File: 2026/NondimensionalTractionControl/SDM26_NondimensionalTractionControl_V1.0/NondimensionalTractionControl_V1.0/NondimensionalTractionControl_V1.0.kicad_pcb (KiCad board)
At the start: 4 copper layers, 50 x 50 mm, 52 parts, among them IC1 STM32H743VIT6, IC2 74LVC1G17SE-7, IC3 TLP175A_TPL,E, IC4 SN65HVD230QDR, IC5 TPS259250DRCR, IC6 MIC37100-3.3WS, IC7 TPS2116DRLR, J1 104031-0811, J2 Conn_ARM_SWD_TagConnect_TC203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, J3 105017-0001, J4 SM04B-ULHK-1TA1-ETB_HF_, J5 SM04B-ULHK-1TA1-ETB_HF_, J6 SM04B-ULHK-1TA1-ETB_HF_, U1 USBLC6-2SC6, Y1 ABM3B-8.000MHZ-10-1-U-T

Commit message: NDTC PCB mostly done
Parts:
- added R12: 10k, Resistor_SMD:R_0603_1608Metric, F.Cu at (158.6, 137.3)
- J3: value 105017-0001 -> USB_B_Micro
- moved R4 81.6 mm to (103.9, 116.3), turned to 180 degrees
- moved J6 66.8 mm to (165.6, 144.2), turned to -90 degrees
- moved C15 65.5 mm to (132.4, 149.0), turned to 180 degrees
- moved C16 61.3 mm to (135.8, 149.0), turned to 180 degrees
- moved C19 57.8 mm to (132.3, 123.3)
- moved R1 57.8 mm to (132.3, 128.3)
- moved C8 55.5 mm to (144.2, 147.5)
- moved C9 54.7 mm to (144.2, 149.0)
- moved R3 54.1 mm to (146.5, 148.2), turned to 90 degrees
- moved R11 53.9 mm to (103.9, 120.2), turned to 180 degrees
- moved R5 50.7 mm to (148.9, 131.0), turned to 180 degrees
- moved R2 43.8 mm to (157.7, 142.0)
- moved R8 43.2 mm to (151.9, 140.6)
- moved C4 43.1 mm to (138.2, 133.0), turned to -90 degrees
- moved C20 41.7 mm to (153.4, 134.2), turned to 180 degrees
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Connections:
- IC1 pad 1: WheelSpeed_2 -> WheelSpeed_3
- IC1 pad 2: WheelSpeed_3 -> WheelSpeed_4
- IC1 pad 3: WheelSpeed_4 -> unconnected-(IC1-PE4-Pad3)
- IC1 pad 51: Net-(IC1-PB12) -> /FDCAN2_RX
- IC1 pad 52: unconnected-(IC1-PB13-Pad52) -> /FDCAN2_TX
- IC1 pad 53: unconnected-(IC1-PB14-Pad53) -> /CAN_TERM
- IC1 pad 54: unconnected-(IC1-PB15-Pad54) -> /USER_LED
- IC1 pad 95: /FDCAN1_RX -> unconnected-(IC1-PB8-Pad95)
- IC1 pad 96: /FDCAN1_TX -> unconnected-(IC1-PB9-Pad96)
- IC1 pad 97: /CAN_TERM -> WheelSpeed_1
- IC1 pad 98: WheelSpeed_1 -> WheelSpeed_2
- IC4 pad 1: /FDCAN1_RX -> /FDCAN2_RX
- IC4 pad 4: /FDCAN1_TX -> /FDCAN2_TX
- IC7 pad 4: GND -> Net-(IC7-PR1)
- J6 pad 1: VCC -> GND
- J6 pad 2: /CAN_HI -> /CAN_LOW
- J6 pad 3: /CAN_LOW -> /CAN_HI
- J6 pad 4: GND -> VCC
- R4 pad 1: Net-(IC1-PB12) -> /USER_LED
- R7 pad 2: GND -> Net-(IC7-PR1)
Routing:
- net GND: track 37.8 -> 100.4 mm, vias 45 -> 73
- net VBUS: track 0.00 -> 37.8 mm, vias 0 -> 3
- net /CAN_HI: track 0.00 -> 16.9 mm
- net /CAN_LOW: track 0.00 -> 16.9 mm
- net +3.3V: track 22.3 -> 37.4 mm, vias 5 -> 11
- net /CAN_TERM: track 0.00 -> 14.3 mm
- net /USB_OTG_DP: track 0.00 -> 13.4 mm
- net /USB_OTG_DM: track 0.00 -> 13.0 mm
- net VCC: track 0.00 -> 12.8 mm
- net Net-(R6-Pad2): track 0.00 -> 12.8 mm
- net Net-(R5-Pad1): track 0.00 -> 12.6 mm
- net +5V: track 0.00 -> 8.76 mm
- net /FDCAN2_RX: track 0.00 -> 8.34 mm
- net Net-(IC4-Rs): track 0.00 -> 6.58 mm
- net Net-(IC7-ST): track 0.00 -> 6.41 mm, vias 0 -> 2
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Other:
- board size 50 x 50 mm -> 70 x 35 mm

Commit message: Computer Sync
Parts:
- added LED3: 150060RS75000, SDM_MiscFootprint:LEDC1608X80N, F.Cu at (155.2, 116.6)
- added R13: 150, Resistor_SMD:R_0603_1608Metric, F.Cu at (155.9, 119.1)
- moved J2 30.5 mm to (175.8, 123.3)
- moved C19 19.0 mm to (148.9, 132.5)
- moved FL1 13.6 mm to (155.8, 123.4), turned to -90 degrees
- moved TP1 7.25 mm to (138.3, 117.1)
- moved R1 3.77 mm to (128.6, 128.9), turned to -90 degrees
- moved R5 1.50 mm to (148.9, 129.5)
- moved R6 1.50 mm to (148.9, 131.0)
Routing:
- net /SDMMC1_CD: track 0.00 -> 37.0 mm
- net /SDMMC1_CMD: track 0.00 -> 28.0 mm
- net /SDMMC1_CK: track 0.00 -> 26.3 mm
- net /SDMMC1_D0: track 0.00 -> 25.6 mm, vias 0 -> 2
- net /SDMMC1_D1: track 0.00 -> 24.9 mm, vias 0 -> 2
- net Net-(FL1-DAT2_EX): track 0.00 -> 13.7 mm
- net Net-(FL1-DAT3_EX): track 0.00 -> 13.4 mm
- net Net-(FL1-DAT1_EX): track 0.00 -> 13.3 mm
- net Net-(FL1-CMD_EX): track 0.00 -> 13.1 mm
- net Net-(FL1-DAT0_EX): track 0.00 -> 13.1 mm
- net Net-(FL1-CLK_EX): track 0.00 -> 12.4 mm
- net +3.3V: track 37.4 -> 43.0 mm, vias 11 -> 14
- net GND: track 100.4 -> 104.9 mm, vias 73 -> 78
- net Net-(IC1-BOOT0): track 2.52 -> 5.03 mm
- net Net-(IC7-ST): track 6.41 -> 8.51 mm
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
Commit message: NTC First Rev Complete
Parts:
- added C21: 100nF, Capacitor_SMD:C_0603_1608Metric, F.Cu at (128.6, 125.9)
- added R14: 10k, Resistor_SMD:R_0603_1608Metric, F.Cu at (139.3, 140.8)
- moved LED2 50.4 mm to (151.7, 116.6), turned to 0 degrees
- moved R11 48.7 mm to (152.6, 119.0), turned to 90 degrees
- moved J2 44.6 mm to (131.4, 126.3), turned to -90 degrees
- moved TP1 17.8 mm to (153.3, 126.6)
- moved C12 0.50 mm to (163.1, 136.6)
- moved IC4 0.10 mm to (144.2, 144.0)
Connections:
- IC1 pad 54: /USER_LED -> unconnected-(IC1-PB15-Pad54)
- IC1 pad 92: unconnected-(IC1-PB6-Pad92) -> /USER_LED
- IC4 pad 1: /FDCAN2_RX -> /FDCAN2_TX
- IC4 pad 4: /FDCAN2_TX -> /FDCAN2_RX
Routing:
- net /USER_LED: track 0.00 -> 31.4 mm, vias 0 -> 2
- net GND: track 104.9 -> 136.3 mm, vias 78 -> 89
- net /SDMMC1_D3: track 0.00 -> 26.5 mm, vias 0 -> 2
- net /SDMMC1_D2: track 0.00 -> 25.9 mm, vias 0 -> 2
- net /Reset: track 0.00 -> 23.3 mm, vias 0 -> 2
- net /SWDIO: track 0.00 -> 17.4 mm, vias 0 -> 2
- net /SWCLK: track 0.00 -> 8.21 mm, vias 0 -> 2
- net /SWO: track 0.00 -> 6.43 mm
- net /FDCAN2_RX: track 8.34 -> 6.13 mm
- net Net-(IC7-ST): track 8.51 -> 10.1 mm
- net VBUS: track 37.8 -> 36.3 mm
- net +3.3V: track 43.0 -> 44.5 mm, vias 14 -> 15
- net /FDCAN2_TX: track 5.23 -> 6.60 mm, vias 2 -> 0
- net /CAN_TERM: track 14.3 -> 15.6 mm

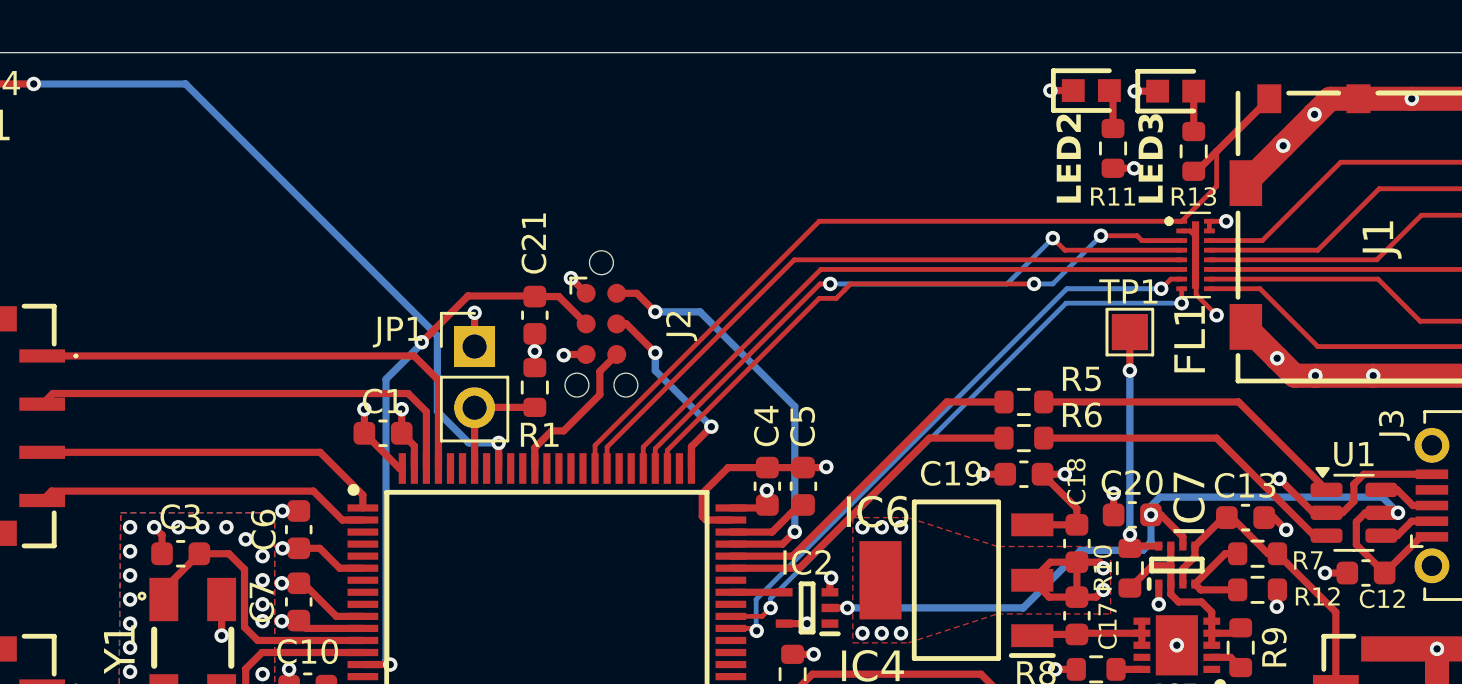
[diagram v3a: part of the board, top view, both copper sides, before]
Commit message: Length matched USB and added mounting holes
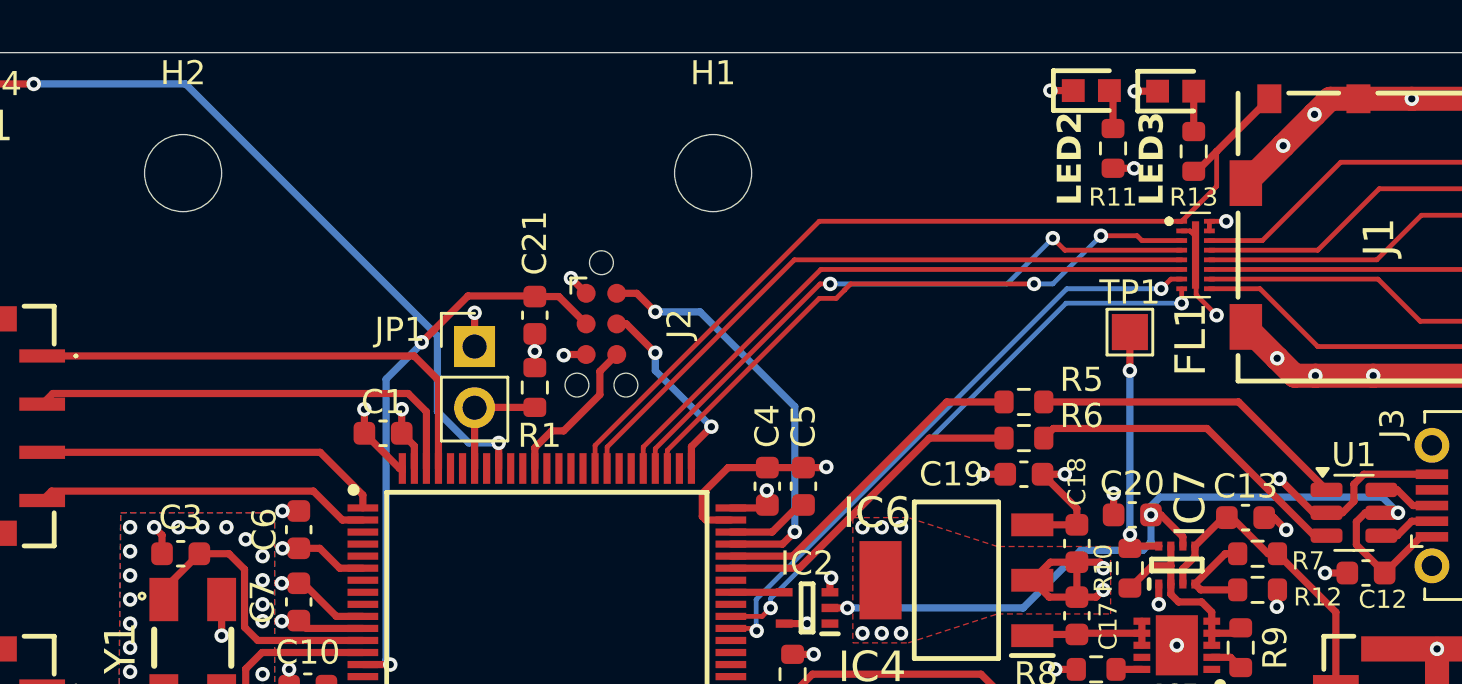
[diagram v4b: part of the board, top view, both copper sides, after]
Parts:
- added H1: M3, MountingHole:MountingHole_3.2mm_M3, F.Cu at (136.0, 120.0)
- added H2: M3, MountingHole:MountingHole_3.2mm_M3, F.Cu at (114.0, 120.0)

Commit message: September order final commit
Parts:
- added C43: 1uF, Capacitor_SMD:C_0603_1608Metric, F.Cu at (152.6, 138.4)
- added R15: 0, Resistor_SMD:R_0603_1608Metric, F.Cu at (153.3, 135.4)
- LED1: value 150060VS75000 -> 150060GS75000
- R11, R13: value 150 -> 68
- R4: value 64.9 -> 5.05
- moved R10 7.85 mm to (154.2, 128.6), turned to 180 degrees
- moved C20 2.24 mm to (155.5, 133.4), turned to 90 degrees
- turned C17 to -90 degrees
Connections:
- C10 pad 1: +3.3V -> +3.3VA
- C11 pad 2: +3.3V -> +3.3VA
- C17 pad 1: Net-(IC5-OUT_1) -> GND
- C17 pad 2: GND -> /EFUSE_OUT
- IC1 pad 20: +3.3V -> +3.3VA
- IC1 pad 21: +3.3V -> +3.3VA
- IC1 pad 28: /MISC_2 -> unconnected-(IC1-PA4-Pad28)
- IC5 pad 6: Net-(IC5-OUT_1) -> /EFUSE_OUT
- IC5 pad 7: Net-(IC5-OUT_1) -> /EFUSE_OUT
- IC5 pad 8: Net-(IC5-OUT_1) -> /EFUSE_OUT
- IC6 pad 1: Net-(IC5-OUT_1) -> /EFUSE_OUT
- J5 pad 1: /ECU_Feedback -> +3.3VA
- J5 pad 2: /MISC_1 -> /ECU_Feedback
- J5 pad 3: /MISC_2 -> /MISC_1
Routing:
- net +3.3VA: track 0.00 -> 19.8 mm
- net /MISC_2: track 18.4 -> 0.00 mm
- net /EFUSE_OUT: track 0.00 -> 9.04 mm
- net +5V: track 8.76 -> 16.4 mm, vias 0 -> 3
- net +3.3V: track 44.5 -> 38.4 mm, vias 15 -> 14
- net Net-(IC5-OUT_1): track 5.59 -> 0.00 mm
- net /ECU_Feedback: track 16.0 -> 14.7 mm
- net VBUS: track 36.3 -> 37.2 mm
- net /MISC_1: track 14.9 -> 14.1 mm
- net Net-(IC7-ST): track 10.1 -> 9.38 mm
- net GND: track 136.3 -> 136.8 mm, vias 89 -> 92
- added copper zone on F.Cu, net +5V
- added copper zone on F.Cu, net /EFUSE_OUT

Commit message: Final Final update for September order
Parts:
- added G***: LOGO, LOGO, F.Cu at (125.4, 118.0)
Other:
- board text added: "SDM-26 DAQ NDTC V1.0"
